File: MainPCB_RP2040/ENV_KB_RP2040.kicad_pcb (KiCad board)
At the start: 2 copper layers, 354.6 x 156.1 mm, 224 parts, among them J2 B3U-1000P, J5 Conn_01x03_Male, U1 TPS63002, U3 RP2040, X1 XO 32 12Mhz 3225 seiko

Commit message: Changed all mount holes to M2 and added some pads around the holes to avoid scratches being visible on pcbs
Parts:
- H0, H1, H10, H3, H4, H6, H7, H9: footprint MountingHole:MountingHole_3.2mm_M3 -> MountingHole:MountingHole_2.2mm_M2_Pad

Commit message: Mostly Completed this design but needs overall improvement
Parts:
- removed I2CHeader0: Conn_01x04, Connector_PinSocket_2.54mm:PinSocket_1x04_P2.54mm_Vertical
- added PowerLED0: LED 0402, LED_SMD:LED_0402_1005Metric, F.Cu at (205.8, 65.6)
- added PowerLedResistor0: 2.2K Resistor 0402, Resistor_SMD:R_0402_1005Metric, F.Cu at (205.8, 67.6)
- moved SW-RST0 20.6 mm to (270.9, 77.3)
- moved C10 3.73 mm to (255.9, 72.9)
- moved R8 0.81 mm to (272.3, 70.3)
- moved LED3 0.78 mm to (274.3, 70.3)
- moved C11 0.74 mm to (269.8, 68.6), turned to 90 degrees
- moved C13 0.65 mm to (259.8, 68.4)
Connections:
- net VBUS renamed USBVBUS
- C10 pad 1: +3V3 -> 3.3V
- C11 pad 1: +3V3 -> 3.3V
- C13 pad 1: +3V3 -> 3.3V
- C14 pad 1: +3V3 -> 3.3V
- C15 pad 1: +3V3 -> 3.3V
- C17 pad 1: +3V3 -> 3.3V
- C4 pad 1: +3V3 -> 3.3V
- C5 pad 1: +3V3 -> 3.3V
- C8 pad 1: +3V3 -> 3.3V
- C9 pad 1: +3V3 -> 3.3V
- FLASH1 pad 8: +3V3 -> 3.3V
- U1 pad 1: +3V3 -> 3.3V
- U1 pad 10: +3V3 -> 3.3V
- U3 pad 1: +3V3 -> 3.3V
- U3 pad 10: +3V3 -> 3.3V
- U3 pad 11: /GPIO8 -> col6
- U3 pad 12: /GPIO9 -> col7
- U3 pad 13: /GPIO10 -> col8
- U3 pad 14: /GPIO11 -> col9
- U3 pad 15: /GPIO12 -> col10
- U3 pad 16: /GPIO13 -> col11
- U3 pad 17: /GPIO14 -> col12
- U3 pad 18: /GPIO15 -> col13
- U3 pad 2: /GPIO0 -> I2CSDA
- U3 pad 22: +3V3 -> 3.3V
- U3 pad 26: /RUN -> Resetbtn
- U3 pad 27: /GPIO16 -> col14
- U3 pad 28: /GPIO17 -> col15
- U3 pad 29: /GPIO18 -> col16
- U3 pad 3: /GPIO1 -> I2CSCL
- U3 pad 30: /GPIO19 -> col17
- U3 pad 31: /GPIO20 -> row0
- U3 pad 32: /GPIO21 -> row2
- U3 pad 33: +3V3 -> 3.3V
- U3 pad 34: /GPIO22 -> row3
- U3 pad 38: /GPIO26_ADC0 -> row4
- U3 pad 39: /GPIO27_ADC1 -> row5
- U3 pad 4: /GPIO2 -> col0
- U3 pad 40: /GPIO28_ADC2 -> row6
- U3 pad 42: +3V3 -> 3.3V
- U3 pad 43: +3V3 -> 3.3V
- U3 pad 44: +3V3 -> 3.3V
- U3 pad 48: +3V3 -> 3.3V
- U3 pad 49: +3V3 -> 3.3V
- U3 pad 5: /GPIO3 -> col1
- U3 pad 6: /GPIO4 -> col2
- U3 pad 7: /GPIO5 -> col3
- U3 pad 8: /GPIO6 -> col4
- U3 pad 9: /GPIO7 -> col5
- X1 pad 4: +3V3 -> 3.3V
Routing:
- net row0: track 316.0 -> 401.8 mm, vias 0 -> 1
- net row2: track 316.2 -> 394.0 mm, vias 0 -> 1
- net row3: track 313.2 -> 389.0 mm, vias 0 -> 1
- net +3V3: track 65.8 -> 0.00 mm, vias 4 -> 0
- net row6: track 308.0 -> 371.8 mm, vias 0 -> 1
- net row4: track 272.1 -> 335.6 mm, vias 0 -> 1
- net row5: track 296.9 -> 356.2 mm, vias 0 -> 1
- net col13: track 137.3 -> 191.5 mm, vias 0 -> 1
- net 3.3V: track 16.1 -> 69.9 mm, vias 1 -> 4
- net GND: track 21.8 -> 58.1 mm, vias 9 -> 17
- net I2CSCL: track 35.9 -> 0.00 mm
- net I2CSDA: track 35.0 -> 0.00 mm
- net col12: track 103.2 -> 131.5 mm, vias 0 -> 1
- net col0: track 354.0 -> 375.2 mm, vias 0 -> 1
- net col16: track 189.2 -> 209.8 mm, vias 0 -> 1
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- added copper zone on F.Cu, net 3.3V
- removed copper zone on F.Cu, net +3V3
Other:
- board text removed: "Reset MCU"
- board text removed: "USB Power"

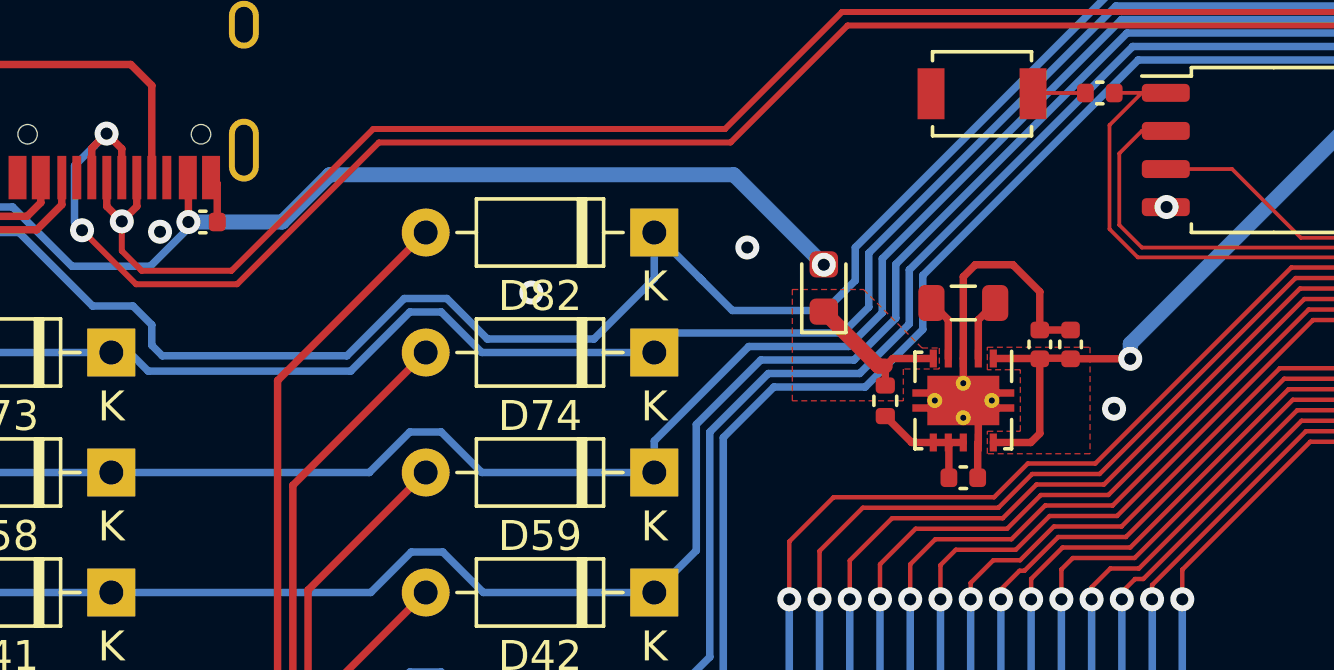
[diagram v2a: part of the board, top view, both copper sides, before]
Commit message: replaced buck boost with a LDO (AP2127K-3.3)
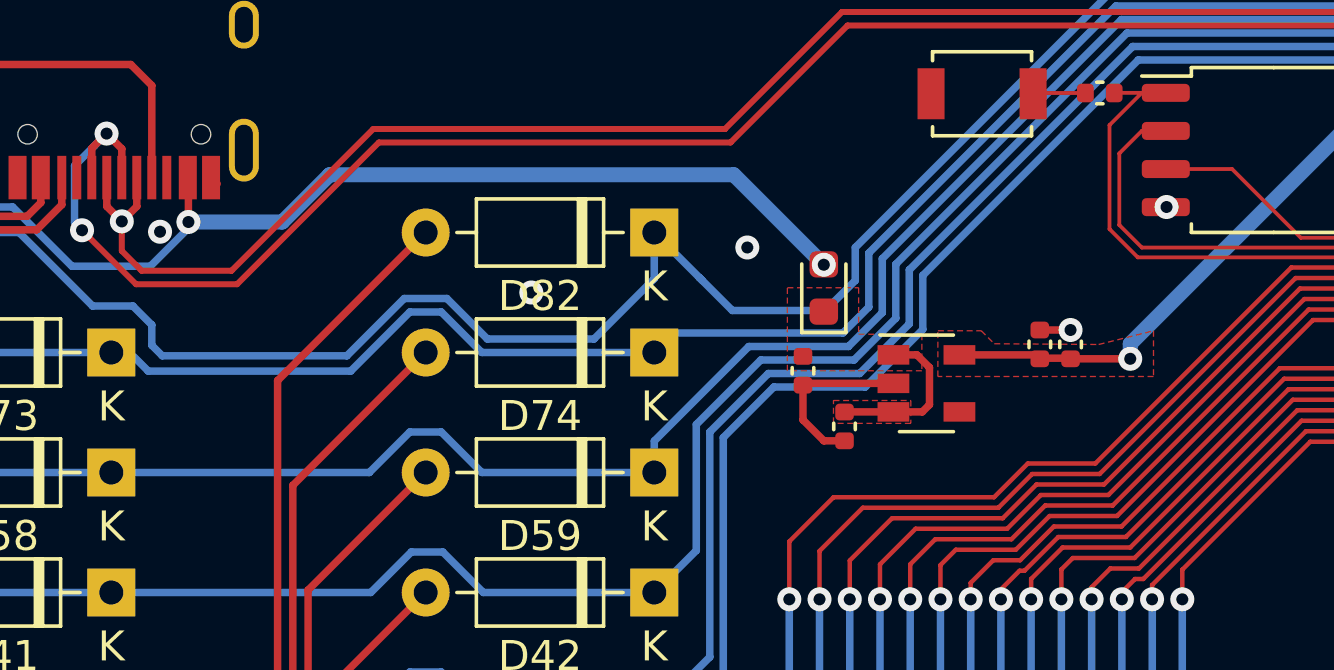
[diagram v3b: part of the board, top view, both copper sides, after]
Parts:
- removed L1: Inductor 2.2uh, Inductor_SMD:L_0805_2012Metric
- removed R7: 100ohm, Resistor_SMD:R_0402_1005Metric
- C12: value 0.1uf 0402 -> 1uF 0402
- U1: value TPS63002 -> AP2127K-3.3; footprint Package_SON:Texas_DRC0010J_ThermalVias -> Package_TO_SOT_SMD:SOT-23-5
- moved C1 20.6 mm to (235.2, 73.8), turned to 270 degrees
- moved C12 4.31 mm to (236.6, 75.6), turned to 270 degrees
- moved U1 1.36 mm to (239.3, 74.2), turned to 0 degrees
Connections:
- C12 pad 1: 3V3_EN -> USBVBUS
- U1 pad 1: 3.3V -> USBVBUS
- U1 pad 2: Net-(L1-Pad2) -> GND
- U1 pad 3: GND -> USBVBUS
- U1 pad 4: Net-(L1-Pad1) -> (no net)
- U1 pad 5: USBVBUS -> 3.3V
- U3 pad 21: /XOUT -> (no net)
- U3 pad 35: /GPIO23 -> (no net)
- U3 pad 36: /GPIO24 -> (no net)
- U3 pad 41: /GPIO29_ADC3 -> (no net)
- X1 pad 1: Net-(X1-Pad1) -> (no net)
- e1 pad 3: Net-(e1-Pad3) -> (no net)
- e1 pad 9: Net-(e1-Pad9) -> (no net)
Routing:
- net GND: track 58.1 -> 51.4 mm
- net 3V3_EN: track 4.15 -> 0.00 mm
- net 3.3V: track 69.9 -> 66.8 mm
- net Net-(L1-Pad2): track 2.08 -> 0.00 mm
- net Net-(L1-Pad1): track 2.08 -> 0.00 mm

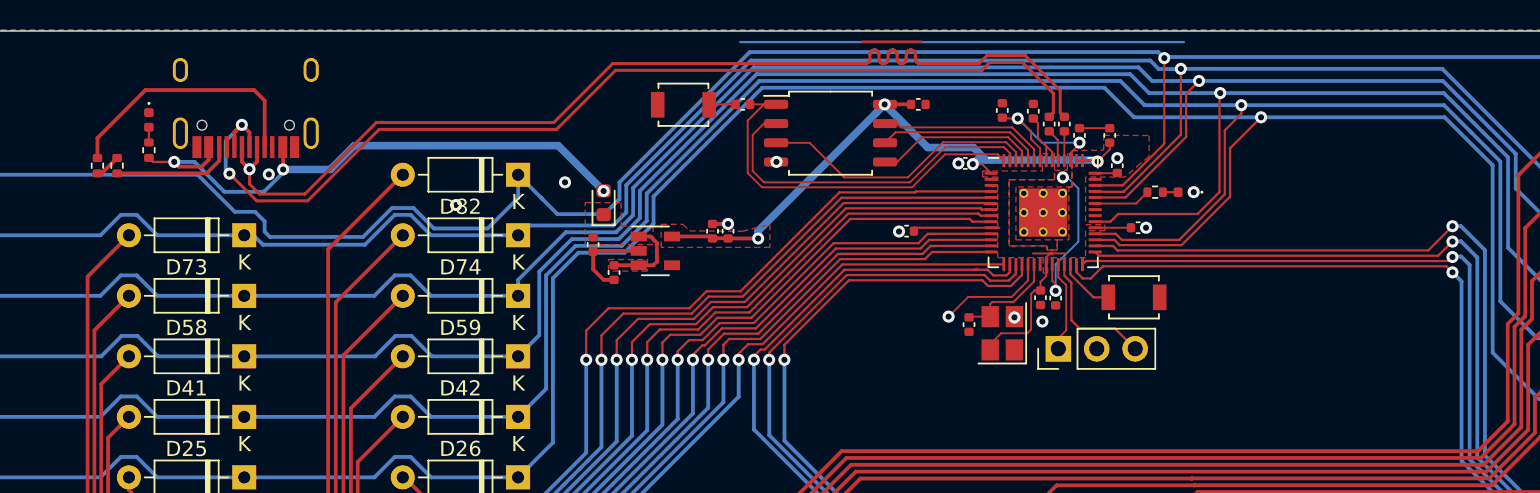
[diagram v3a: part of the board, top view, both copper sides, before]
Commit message: corrected all DRC Errors, all vias on pads as well as separated vbus and vsys in the schematic properly.
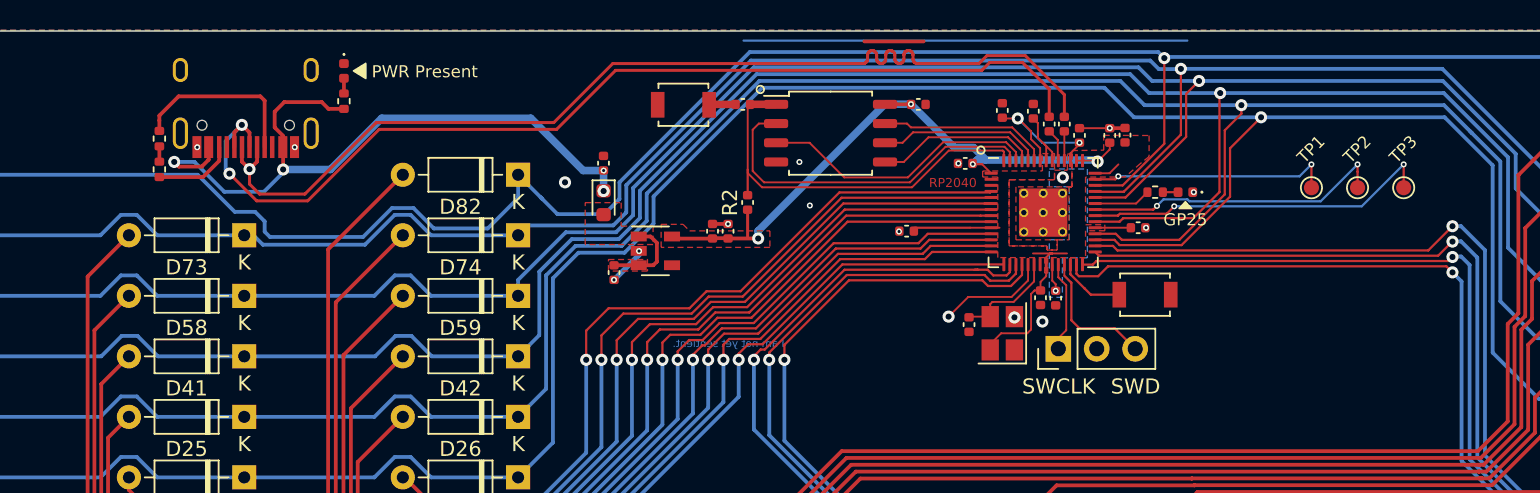
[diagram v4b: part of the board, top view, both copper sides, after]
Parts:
- added R2: DNF, Capacitor_SMD:C_0402_1005Metric, F.Cu at (245.4, 71.0)
- added TP1: TestPoint, TestPoint:TestPoint_Pad_D1.0mm, F.Cu at (282.7, 70.0)
- added TP2: TestPoint, TestPoint:TestPoint_Pad_D1.0mm, F.Cu at (285.7, 70.0)
- added TP3: TestPoint, TestPoint:TestPoint_Pad_D1.0mm, F.Cu at (288.8, 70.0)
- moved PowerLED0 13.3 mm to (218.7, 62.3)
- moved PowerLedResistor0 13.3 mm to (218.7, 64.3)
- moved C1 5.42 mm to (235.9, 68.4), turned to 90 degrees
- moved R5 4.47 mm to (206.5, 66.8)
- moved R6 2.80 mm to (206.5, 68.8)
- moved C11 2.08 mm to (270.3, 66.6)
- moved SW-RST0 0.75 mm to (271.7, 77.1)
- turned Diode1 to 270 degrees
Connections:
- C12 pad 1: USBVBUS -> VSYS
- Diode1 pad 2: USBVBUS -> VSYS
- U1 pad 1: USBVBUS -> VSYS
- U1 pad 3: USBVBUS -> VSYS
- U1 pad 4: (no net) -> Net-(U1-Pad4)
- U3 pad 21: (no net) -> /XOUT
- U3 pad 35: (no net) -> /GPIO23
- U3 pad 36: (no net) -> /GPIO24
- U3 pad 41: (no net) -> /GPIO29_ADC3
- X1 pad 1: (no net) -> Net-(X1-Pad1)
- e1 pad 3: (no net) -> Net-(e1-Pad3)
- e1 pad 9: (no net) -> Net-(e1-Pad9)
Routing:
- net /GPIO23: track 0.00 -> 23.3 mm, vias 0 -> 2
- net /GPIO24: track 0.00 -> 20.2 mm, vias 0 -> 2
- net /GPIO29_ADC3: track 0.00 -> 16.2 mm, vias 0 -> 2
- net +1V1: track 21.2 -> 12.4 mm
- net VSYS: track 0.00 -> 5.62 mm
- net Net-(R5-Pad2): track 17.0 -> 11.7 mm
- net GND: track 51.4 -> 48.2 mm, vias 17 -> 21
- net Net-(R6-Pad2): track 8.00 -> 5.31 mm
- net USBVBUS: track 44.1 -> 46.6 mm, vias 3 -> 4
- net 3.3V: track 66.8 -> 69.0 mm
- net /QSPI_SS: track 25.9 -> 27.0 mm
- net Resetbtn: track 3.77 -> 4.43 mm
- net (no net): vias 1 -> 0
- added copper zone on B.Cu, net +1V1
- added copper zone on F.Cu, net VSYS
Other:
- net class DIFF: via_dia 0.8 -> 0.4; via_drill 0.4 -> 0.2
- net class Default: clearance 0.2 -> 0.127; via_dia 0.8 -> 0.4; via_drill 0.4 -> 0.2
- rule pad_to_mask_clearance: 0.051 -> 0
- rule trace_clearance: 0.2 -> 0.127
- rule via_min_drill: 0.3 -> 0.2
- board text added: "GP25"
- board text added: "I am not yet sentient."
- board text added: "PWR Present"
- board text added: "RP2040"
- board text added: "SWCLK"
- board text added: "SWD"

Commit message: corrected a couple of small issues
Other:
- board text added: "GP23"
- board text added: "GP24"
- board text added: "GP29"

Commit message: some tweaks and corrections, fixed some issues on rp2040 version
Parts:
- removed TP1, TP2, TP3: TestPoint, TestPoint:TestPoint_Pad_D1.0mm
- added G***: LOGO, EnvExtras:RPIlogo, F.Cu at (285.0, 76.8)
- moved C17 0.20 mm to (271.2, 72.5)
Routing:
- net /GPIO23: track 23.3 -> 0.00 mm, vias 2 -> 0
- net /GPIO24: track 20.2 -> 0.00 mm, vias 2 -> 0
- net /GPIO29_ADC3: track 16.2 -> 0.00 mm, vias 2 -> 0
- net col17: track 229.1 -> 221.2 mm
- net col16: track 209.8 -> 202.0 mm
- net col15: track 188.5 -> 181.1 mm
- net GND: track 48.2 -> 55.4 mm
- net col14: track 206.8 -> 199.9 mm
- added copper zone on B.Cu, net 3.3V
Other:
- board text removed: "3V3"
- board text removed: "GND"
- board text removed: "GP23"
- board text removed: "GP24"
- board text removed: "GP29"
- board text removed: "SCL"
- board text removed: "SDA"
